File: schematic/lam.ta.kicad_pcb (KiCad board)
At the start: 2 copper layers, 91.4 x 91.4 mm, 16 parts, among them J1 Arduino_Nano_Header, P1 CONN_LED0, P10 CONN_TOUCH3, P2 CONN_LED1, P3 CONN_LED2, P4 CONN_LED3, P5 CONN_PSU, P6 CONN_LINE_IN, P7 CONN_TOUCH0, P8 CONN_TOUCH1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

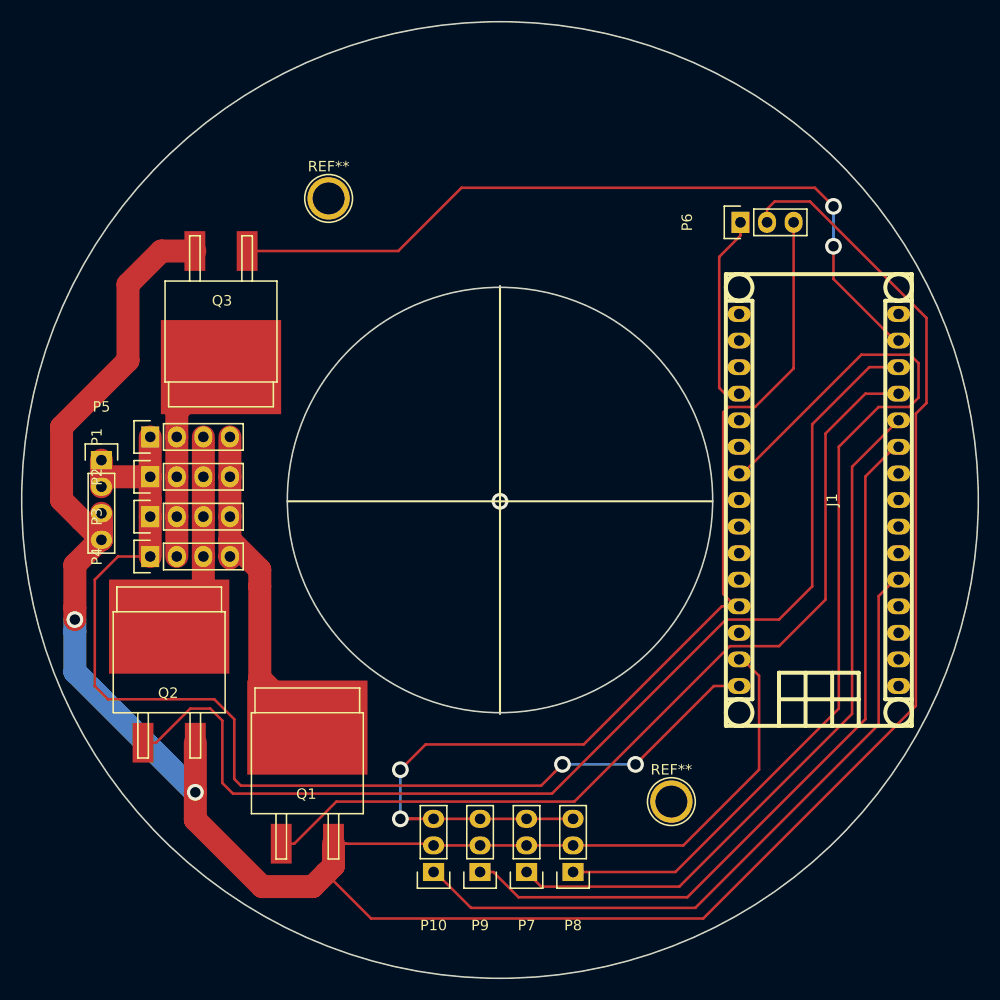
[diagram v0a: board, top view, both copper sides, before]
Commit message: Update schematic license, replace AT42QT101X with MPR121
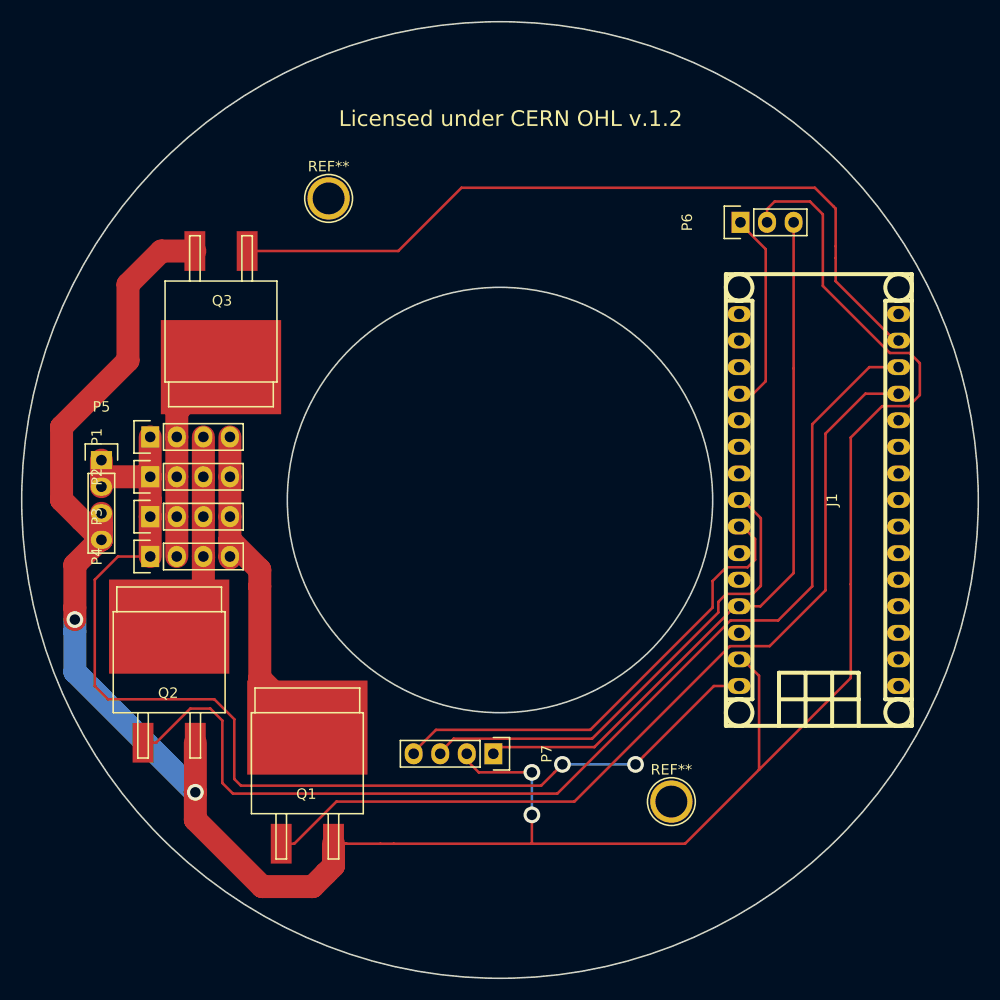
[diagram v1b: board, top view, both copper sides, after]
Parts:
- removed P10: CONN_TOUCH3, Pin_Headers:Pin_Header_Straight_1x03
- removed P8: CONN_TOUCH1, Pin_Headers:Pin_Header_Straight_1x03
- removed P9: CONN_TOUCH2, Pin_Headers:Pin_Header_Straight_1x03
- P7: value CONN_TOUCH0 -> CONN_MPR121; footprint Pin_Headers:Pin_Header_Straight_1x03 -> Pin_Headers:Pin_Header_Straight_1x04
- moved P7 11.7 mm to (151.0, 111.8), turned to 270 degrees
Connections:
- J1 pad 10: TOUCH2 -> Net-(J1-Pad10)
- J1 pad 11: TOUCH0 -> Net-(J1-Pad11)
- J1 pad 22: TOUCH1 -> Net-(J1-Pad22)
- J1 pad 5: TOUCH3 -> Net-(J1-Pad5)
- P7 pad 1: TOUCH0 -> +5V
- P7 pad 3: +5V -> Net-(J1-Pad23)
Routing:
- net TOUCH1: track 91.9 -> 0.00 mm
- net TOUCH2: track 72.4 -> 0.00 mm
- net TOUCH0: track 68.4 -> 0.00 mm
- net TOUCH3: track 66.1 -> 0.00 mm
- net Net-(J1-Pad23): track 0.00 -> 47.2 mm
- net Net-(J1-Pad24): track 0.00 -> 45.9 mm
- net GND: track 278.0 -> 239.8 mm, vias 2 -> 4
- net +5V: track 103.8 -> 69.8 mm, vias 2 -> 0
- net PWM_BLUE: track 86.1 -> 85.6 mm
- net PWM_GREEN: vias 2 -> 0
- net (no net): vias 1 -> 0
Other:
- board text added: "Copyright 2016 Nicola Corna <nicola@corna.info> This documentation describes Open Hardware and is licensed under the CERN OHL v. 1.2. You may redistribute and modify this documentation under the terms of the CERN OHL v.1.2. (http://ohwr.org/cernohl). This documentation is distributed WITHOUT ANY EXPRESS OR IMPLIED WARRANTY, INCLUDING OF MERCHANTABILITY, SATISFACTORY QUALITY AND FITNESS FOR A PART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"
- board text added: "Licensed under CERN OHL v.1.2"
